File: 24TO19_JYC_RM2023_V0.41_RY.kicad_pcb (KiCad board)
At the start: 2 copper layers, 35 x 68.2 mm, 41 parts, among them J1 Conn_01x02, Q1 BSC070N10NS5, Q2 BSC070N10NS5, U1 LM3150MH

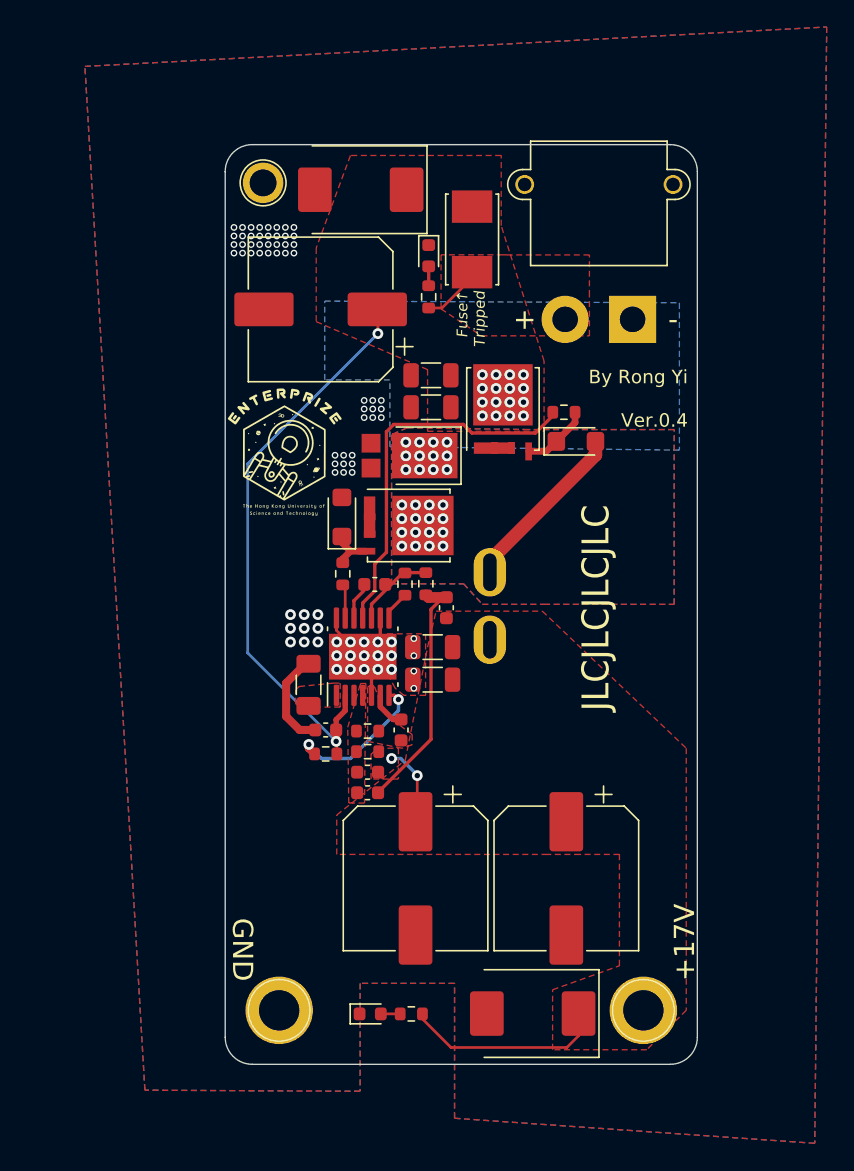
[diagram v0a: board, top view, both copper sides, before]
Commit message: Updating to ver 0.41: Changed Caps to THT; Decreased total area. Layout done. Routing pending.
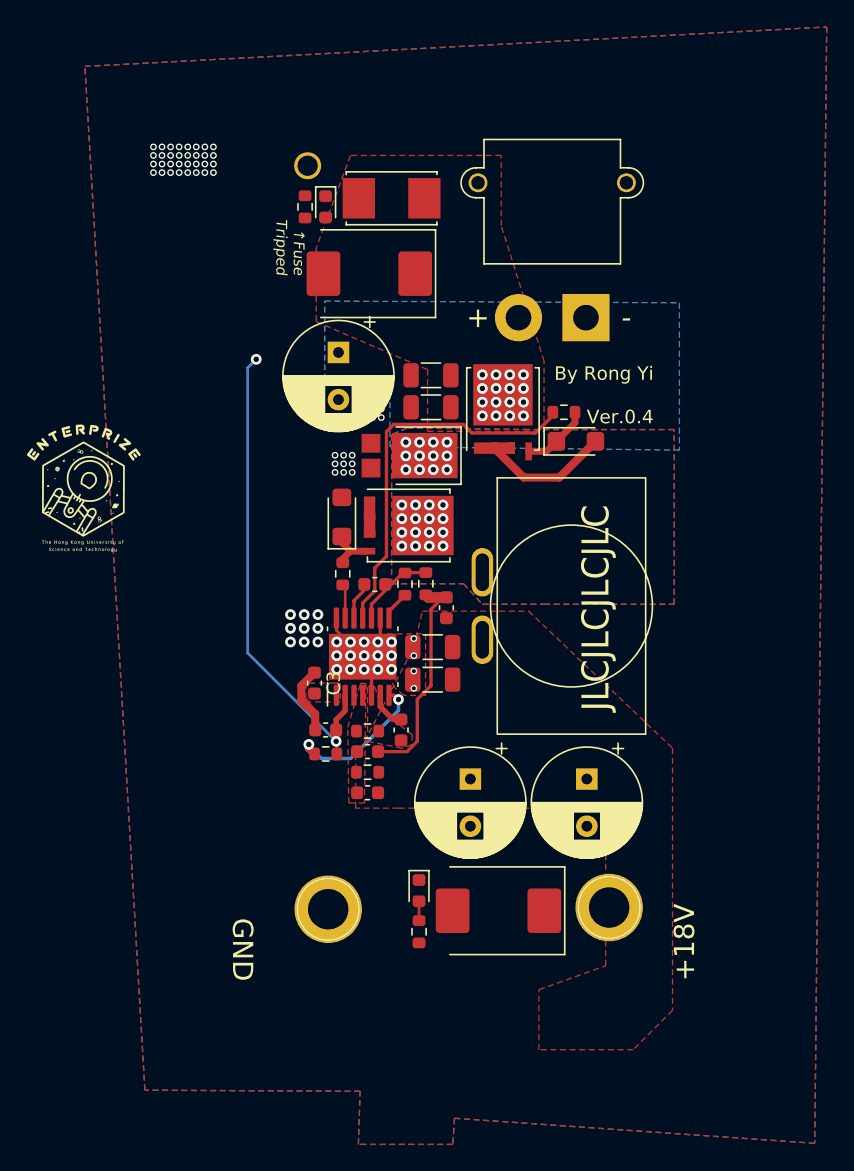
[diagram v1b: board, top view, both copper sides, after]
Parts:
- C10, C12, C13, C9: value 100uF -> 22uF
- C11, C4: value 100uF -> 330uF; footprint Capacitor_SMD:CP_Elec_10x10.5 -> Capacitor_THT:CP_Radial_D8.0mm_P3.50mm
- C3: footprint Capacitor_SMD:C_1206_3216Metric_Pad1.33x1.80mm_HandSolder -> Capacitor_SMD:C_0603_1608Metric
- C6: value 100uF -> 220uF; footprint Capacitor_SMD:CP_Elec_10x10.5 -> Capacitor_THT:CP_Radial_D8.0mm_P3.50mm
- L1: value 10uh -> 4.7uH
- moved G*** 15.1 mm to (111.1, 80.1)
- moved R6 11.3 mm to (127.7, 59.4), turned to -90 degrees
- moved D3 9.83 mm to (136.1, 110.1), turned to -90 degrees
- moved D7 8.45 mm to (129.2, 59.4)
- moved C11 8.41 mm to (140.0, 101.9)
- moved TP1 8.33 mm to (129.4, 111.5)
- moved D1 8.03 mm to (142.0, 111.6)
- moved TP2 8.03 mm to (150.2, 111.4)
- moved C4 7.52 mm to (148.6, 101.9)
- moved F1 6.70 mm to (134.1, 58.8), turned to 0 degrees
- moved D2 6.26 mm to (132.5, 64.4)
- moved R9 6.12 mm to (136.1, 113.2), turned to 90 degrees
- moved TP3 3.54 mm to (127.9, 56.4)
- moved J1 3.46 mm to (148.5, 67.7)
- moved C6 3.45 mm to (130.2, 70.2), turned to -90 degrees
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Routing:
- net /VOUT: track 22.6 -> 0.03 mm, vias 2 -> 0
- net +24V: track 43.4 -> 35.9 mm
- net Net-(J1-Pin_2): track 4.56 -> 0.00 mm
- net /SW: track 19.0 -> 15.5 mm
- net GND: track 14.7 -> 12.5 mm
- net Net-(C7-Pad2): track 18.2 -> 16.4 mm
- net Net-(D7-A): track 1.44 -> 0.00 mm
- removed copper zone on F.Cu, net Net-(J1-Pin_2)
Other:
- board outline removed
- board text added: "+18V"
- board text added: "↑Fuse Tripped"
- board text removed: "+17V"
- board text removed: "Fuse↑ Tripped"

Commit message: v0.41 done
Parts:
- removed the G*** at (111.1, 80.1)
- added D8: SMF12A, Diode_SMD:D_SMF, F.Cu at (136.0, 111.9)
- D1: value SMAJ18A -> SMCJ18A
- R3, R4: value 4.7r -> 3.3R
- R6: value 274K -> 100K
- R7: value 274K -> 287K
- R9: value 274K -> 1K
- moved G*** 23.8 mm to (135.1, 60.8), turned to -90 degrees
- moved R6 8.48 mm to (135.5, 56.1), turned to 180 degrees
- moved D7 4.62 mm to (132.5, 56.1), turned to 0 degrees
- moved D3 4.32 mm to (133.3, 113.4), turned to 0 degrees
- moved R9 3.03 mm to (134.0, 111.0), turned to -90 degrees
- moved TP3 2.11 mm to (127.8, 58.5)
- moved D2 1.14 mm to (133.6, 64.4)
- moved C2 0.99 mm to (135.6, 97.7)
- moved J1 0.98 mm to (148.5, 66.7)
- moved R1 0.95 mm to (129.4, 99.1), turned to 180 degrees
- moved C14 0.92 mm to (133.1, 102.4)
- moved C7 0.92 mm to (133.1, 99.3)
- moved R7 0.92 mm to (133.1, 100.8)
- moved R8 0.92 mm to (133.1, 97.8)
- moved Q1 0.79 mm to (142.2, 75.2)
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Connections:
- R9 pad 1: /VOUT -> Net-(D8-A2)
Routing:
- net GND: track 12.5 -> 43.6 mm, vias 78 -> 79
- net Net-(J1-Pin_2): track 0.00 -> 14.5 mm
- net /VOUT: track 0.03 -> 10.7 mm
- net FB: track 0.00 -> 6.86 mm
- net Net-(U1-RON): track 11.1 -> 6.47 mm
- net +24V: track 35.9 -> 38.2 mm, vias 18 -> 1
- net Net-(D8-A2): track 0.00 -> 2.11 mm
- net Net-(D7-A): track 0.00 -> 1.44 mm
- net Net-(C7-Pad2): track 16.4 -> 15.5 mm
- net /HO: track 28.1 -> 28.9 mm
- net Net-(U1-SS): track 2.78 -> 3.37 mm
- net /SW: track 15.5 -> 15.7 mm, vias 28 -> 0
- removed copper zone on F.Cu, net FB
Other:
- board outline added: 28 x 60 mm
- board text added: "24V→18V DCDC Module MiniPC Power Supply 8A MAX RM202'3'"
- board text added: "By Rong Yi Ver.0.41"
- board text added: "SW"
- board text added: "VIN"
- board text removed: "24V→17V DCDC Module MiniPC Power Supply 10A MAX RM2023"
- board text removed: "By Rong Yi Ver.0.4"
- board text removed: "↑Fuse Tripped"
